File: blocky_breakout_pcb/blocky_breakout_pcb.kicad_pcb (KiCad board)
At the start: 4 copper layers, 85 x 61 mm, 91 parts, among them J1 Raspberry_Pi_4, J10 Conn_01x02_Pin, J11 Conn_01x02_Pin, J12 Conn_01x02_Pin, J2 USB_C_Receptacle_USB2.0_16P, J3 Conn_01x14_Pin, J4 Conn_01x08_Pin, J5 Conn_01x10_Pin, J6 Conn_01x06_Pin, J7 Conn_01x08_Pin, J9 Conn_01x03_Pin, K1 EE2-3TNUH, K2 EE2-3TNUH, Q1 DMG1012TQ-7, Q2 DMG1012TQ-7, SW1 SW_Push, SW2 SW_DIP_x04, U1 W25Q32JVSS, U2 NUP2202, U3 RP2350, U4 LM4040C33FTA, U5 LM66100DCK, U6 AOZ1280CI, U7 LM66100DCK, U8 MCP4728, U9 TCR2EE11, Y1 12Mhz

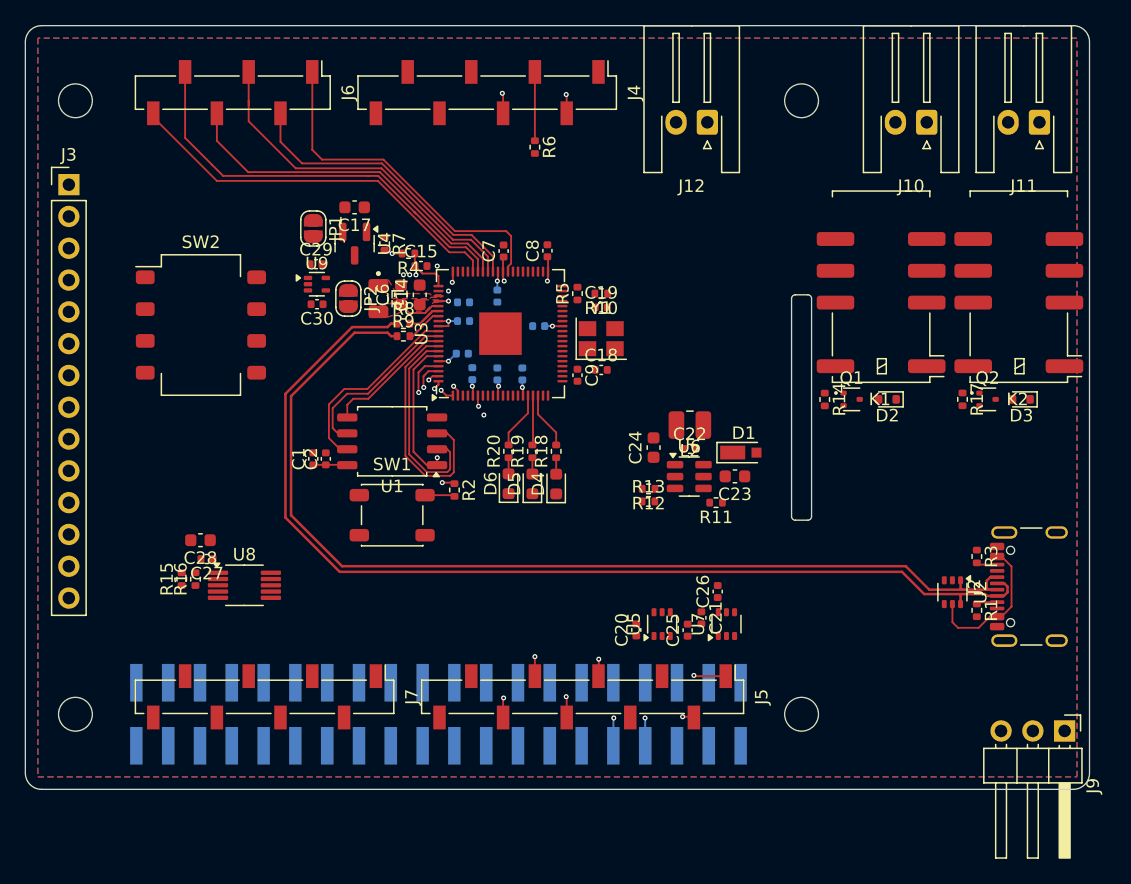
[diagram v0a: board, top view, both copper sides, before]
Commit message: Layout nearly finished, entering part numbers
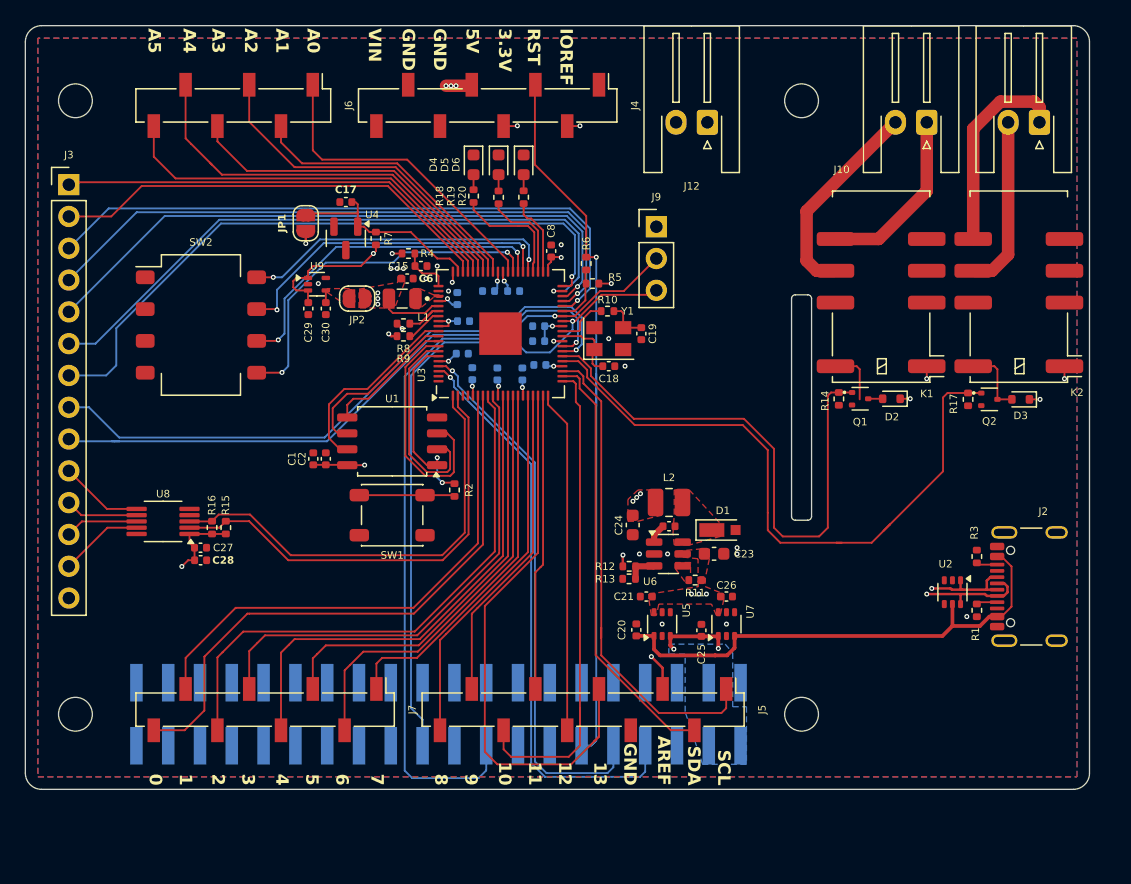
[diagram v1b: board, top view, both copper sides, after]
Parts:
- C14: footprint Capacitor_SMD:C_0603_1608Metric -> Capacitor_SMD:C_0402_1005Metric; moved to B.Cu
- C17, C28, C6: footprint Capacitor_SMD:C_0603_1608Metric -> Capacitor_SMD:C_0402_1005Metric
- C2: value 10nF -> 100nF
- C7, C9: moved to B.Cu
- J9: footprint Connector_PinHeader_2.54mm:PinHeader_1x03_P2.54mm_Horizontal -> Connector_PinHeader_2.54mm:PinHeader_1x03_P2.54mm_Vertical
- Y1: footprint Crystal:Crystal_SMD_Abracon_ABM8AIG-4Pin_3.2x2.5mm -> X_Abracon:Crystal_SMD_Abracon_ABM8-272-T3-4Pin_3.2x2.5mm
- moved J9 51.8 mm to (151.4, 82.1), turned to 0 degrees
- moved D4 26.3 mm to (136.8, 77.1), turned to -90 degrees
- moved D5 25.6 mm to (138.8, 77.1), turned to -90 degrees
- moved D6 25.5 mm to (140.8, 77.1), turned to -90 degrees
- moved R18 21.4 mm to (136.8, 79.6), turned to -90 degrees
- moved R19 20.5 mm to (138.8, 79.7), turned to -90 degrees
- moved R20 20.3 mm to (140.8, 79.7), turned to -90 degrees
- moved R6 10.2 mm to (145.8, 85.0)
- moved U8 8.26 mm to (112.0, 105.6), turned to 180 degrees
- moved C16 6.75 mm to (142.0, 91.2), turned to 180 degrees
- moved C22 6.41 mm to (152.4, 106.0)
- moved C23 6.41 mm to (156.0, 108.2)
- moved C24 6.41 mm to (149.5, 105.9)
- moved D1 6.41 mm to (156.7, 106.3)
- moved R11 6.41 mm to (154.5, 110.3)
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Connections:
- J1 pad 11: /RP2350/SWD_SWDIO -> unconnected-(J1-GPIO17/SPI1_~{CE1}-Pad11)
- J1 pad 18: unconnected-(J1-GPIO24/SDIO_DAT0-Pad18) -> /RP2350/SWD_SWDIO
- J1 pad 22: unconnected-(J1-GPIO25/SDIO_DAT1-Pad22) -> /RP2350/SWD_SWCLK
- J1 pad 36: /RP2350/SWD_SWCLK -> unconnected-(J1-GPIO16/SPI1_~{CE2}-Pad36)
- J3 pad 1: /RP2350/GPIO6 -> /RP2350/GPIO46
- J3 pad 10: /RP2350/GPIO30 -> /DAC/DAC0
- J3 pad 11: /RP2350/GPIO31 -> /DAC/DAC1
- J3 pad 12: /RP2350/GPIO46 -> /DAC/DAC2
- J3 pad 13: /RP2350/GPIO47 -> /DAC/DAC3
- J3 pad 2: /RP2350/GPIO7 -> /RP2350/GPIO47
- J3 pad 3: /RP2350/GPIO19 -> /RP2350/GPIO28
- J3 pad 4: /RP2350/GPIO23 -> /RP2350/GPIO29
- J3 pad 5: /RP2350/GPIO22 -> /RP2350/GPIO30
- J3 pad 6: /RP2350/GPIO26 -> /RP2350/GPIO31
- J3 pad 7: /RP2350/GPIO27 -> /RP2350/GPIO32
- J3 pad 8: /RP2350/GPIO28 -> /RP2350/GPIO26
- J3 pad 9: /RP2350/GPIO29 -> /RP2350/GPIO27
- J5 pad 1: /Arduino Headers/I2C0.SCL -> /Arduino Headers/I2C1.SCL
- J5 pad 2: /Arduino Headers/I2C0.SDA -> /Arduino Headers/I2C1.SDA
- Q1 pad 1: /RP2350/RELAY1_EN -> /RP2350/RELAY2_EN
- Q2 pad 1: /RP2350/RELAY2_EN -> /RP2350/RELAY1_EN
- R14 pad 1: /RP2350/RELAY1_EN -> /RP2350/RELAY2_EN
- R15 pad 1: /DAC/I2C1.SCL -> /DAC/I2C0.SCL
- R16 pad 1: /DAC/I2C1.SDA -> /DAC/I2C0.SDA
- R17 pad 1: /RP2350/RELAY2_EN -> /RP2350/RELAY1_EN
- R18 pad 2: /RP2350/GPIO18 -> /RP2350/GPIO35
- R19 pad 2: /RP2350/GPIO17 -> /RP2350/GPIO34
- R20 pad 2: /RP2350/GPIO16 -> /RP2350/GPIO33
- SW2 pad 5: /RP2350/GPIO12 -> /RP2350/GPIO39
- SW2 pad 6: /RP2350/GPIO13 -> /RP2350/GPIO38
- SW2 pad 7: /RP2350/GPIO14 -> /RP2350/GPIO37
- SW2 pad 8: /RP2350/GPIO15 -> /RP2350/GPIO36
- U3 pad 1: /Arduino Headers/SPI0.MISO -> /DAC/I2C0.SDA
- U3 pad 11: /RP2350/GPIO12 -> /Arduino Headers/D4
- U3 pad 12: /RP2350/GPIO13 -> /Arduino Headers/D5
- U3 pad 13: /RP2350/GPIO14 -> /Arduino Headers/D6
- U3 pad 14: /RP2350/GPIO15 -> /Arduino Headers/D7
- U3 pad 16: /RP2350/GPIO16 -> /Arduino Headers/D8
- U3 pad 17: /RP2350/GPIO17 -> /Arduino Headers/D9
- U3 pad 18: /RP2350/GPIO18 -> /Arduino Headers/SPI0.SCK
- U3 pad 19: /RP2350/GPIO19 -> /Arduino Headers/SPI0.MOSI
- U3 pad 2: /Arduino Headers/SPI0.CS -> /DAC/I2C0.SCL
- U3 pad 20: /Arduino Headers/D0/RX -> /Arduino Headers/SPI0.MISO
- U3 pad 21: /Arduino Headers/D1/TX -> /Arduino Headers/SPI0.CS
- U3 pad 22: /RP2350/GPIO22 -> /Arduino Headers/I2C1.SDA
- U3 pad 23: /RP2350/GPIO23 -> /Arduino Headers/I2C1.SCL
- U3 pad 40: /Arduino Headers/D2 -> /RP2350/GPIO32
- U3 pad 42: /Arduino Headers/D3 -> /RP2350/GPIO33
- U3 pad 43: /Arduino Headers/D4 -> /RP2350/GPIO34
- U3 pad 44: /Arduino Headers/D5 -> /RP2350/GPIO35
- U3 pad 45: /Arduino Headers/D6 -> /RP2350/GPIO36
- U3 pad 46: /Arduino Headers/D7 -> /RP2350/GPIO37
- U3 pad 47: /Arduino Headers/D8 -> /RP2350/GPIO38
- U3 pad 48: /Arduino Headers/D9 -> /RP2350/GPIO39
- U3 pad 6: /Arduino Headers/I2C0.SDA -> /Arduino Headers/D1/TX
- U3 pad 7: /Arduino Headers/I2C0.SCL -> /Arduino Headers/D0/RX
- U3 pad 79: /Arduino Headers/SPI0.SCK -> unconnected-(U3B-GPIO2-Pad79)
- U3 pad 8: /DAC/I2C1.SDA -> /Arduino Headers/D2
- U3 pad 80: /Arduino Headers/SPI0.MOSI -> unconnected-(U3B-GPIO3-Pad80)
- U3 pad 9: /DAC/I2C1.SCL -> /Arduino Headers/D3
- U8 pad 2: /DAC/I2C1.SCL -> /DAC/I2C0.SCL
- U8 pad 3: /DAC/I2C1.SDA -> /DAC/I2C0.SDA
- U8 pad 6: unconnected-(U8-VOUTA-Pad6) -> /DAC/DAC0
- U8 pad 7: unconnected-(U8-VOUTB-Pad7) -> /DAC/DAC1
- U8 pad 8: unconnected-(U8-VOUTC-Pad8) -> /DAC/DAC2
- U8 pad 9: unconnected-(U8-VOUTD-Pad9) -> /DAC/DAC3
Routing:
- net +5V: track 0.00 -> 72.2 mm, vias 0 -> 7
- net /RP2350/SWD_SWDIO: track 0.00 -> 64.5 mm, vias 0 -> 1
- net /RP2350/SWD_SWCLK: track 0.00 -> 54.3 mm, vias 0 -> 1
- net /Arduino Headers/RST: track 5.49 -> 59.1 mm, vias 0 -> 1
- net /RP2350/RELAY1_EN: track 0.00 -> 53.1 mm
- net /RP2350/GPIO32: track 0.00 -> 52.4 mm, vias 0 -> 1
- net /RP2350/GPIO31: track 0.00 -> 51.9 mm, vias 0 -> 1
- net /RP2350/GPIO28: track 0.00 -> 51.2 mm, vias 0 -> 1
- net /RP2350/GPIO29: track 0.00 -> 51.0 mm, vias 0 -> 1
- net /RP2350/GPIO30: track 0.00 -> 50.8 mm, vias 0 -> 1
- net /RP2350/GPIO26: track 0.00 -> 50.6 mm, vias 0 -> 1
- net /RP2350/GPIO27: track 0.00 -> 49.1 mm, vias 0 -> 1
- net /Arduino Headers/AREF: track 0.00 -> 48.4 mm, vias 0 -> 2
- net /Arduino Headers/D0/RX: track 0.00 -> 46.9 mm
- net /Arduino Headers/D2: track 0.00 -> 44.2 mm
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- added copper zone on In1.Cu, net +1V1
- added copper zone on F.Cu, net +5V
- added copper zone on B.Cu, net +5V_RPI
- added copper zone on F.Cu, net Net-(D1-K)
- added copper zone on F.Cu, net Net-(JP2-A)
- added copper zone on F.Cu, net Net-(U6-EN)
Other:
- board text added: "0"
- board text added: "1"
- board text added: "10"
- board text added: "11"
- board text added: "12"
- board text added: "13"
- board text added: "2"
- board text added: "3"
- board text added: "3.3V"
- board text added: "4"
- board text added: "5"
- board text added: "5V"
- board text added: "6"
- board text added: "7"
- board text added: "8"
- board text added: "9"
- board text added: "A0"
- board text added: "A1"
- board text added: "A2"
- board text added: "A3"
- board text added: "A4"
- board text added: "A5"
- board text added: "AREF"
- board text added: "GND"
- board text added: "IOREF"
- board text added: "RST"
- board text added: "SCL"
- board text added: "SDA"
- board text added: "VIN"

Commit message: Added some docs, worked on routing.
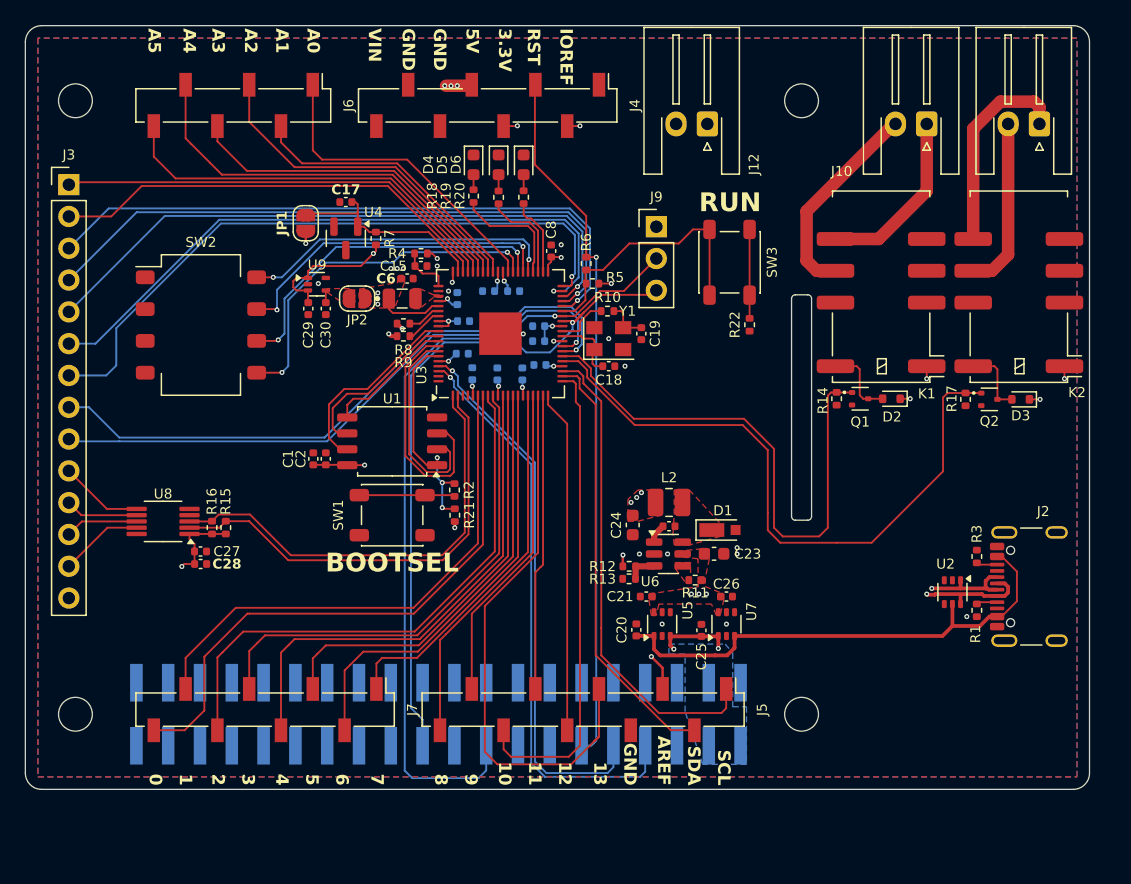
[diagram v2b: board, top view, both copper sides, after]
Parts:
- added R21: 10k, Resistor_SMD:R_0402_1005Metric, F.Cu at (135.3, 105.1)
- added R22: 1k, Resistor_SMD:R_0402_1005Metric, F.Cu at (158.8, 89.9)
- added SW3: SW_Push, Button_Switch_SMD:SW_SPST_PTS647_Sx38, F.Cu at (157.2, 84.9)
- moved R4 1.00 mm to (132.6, 84.2), turned to 0 degrees
- moved C27 0.30 mm to (115.0, 108.0)
- moved C28 0.30 mm to (115.0, 109.0)
- moved R17 0.20 mm to (176.1, 95.8)
- moved R14 0.18 mm to (165.8, 95.8)
- moved J10 0.13 mm to (173.0, 73.8)
- moved J11 0.13 mm to (182.0, 73.8)
- moved J12 0.13 mm to (155.5, 73.8)
- turned L1 to 0 degrees
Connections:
- L1 pad 1: /RP2350/VREF_LX -> +1V1
- L1 pad 2: +1V1 -> /RP2350/VREF_LX
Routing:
- net Net-(U3A-RUN): track 4.65 -> 21.1 mm
- net Net-(R22-Pad2): track 0.00 -> 7.10 mm
- net /RP2350/QSPI_~{SS}: track 15.1 -> 18.1 mm, vias 2 -> 3
- net /RP2350/SWD_SWCLK: track 54.3 -> 57.3 mm
- net /Arduino Headers/RST: track 59.1 -> 56.5 mm
- net /Arduino Headers/SPI0.CS: track 41.1 -> 39.1 mm
- net Net-(U3A-USB_DM): track 3.84 -> 2.70 mm
- net /RP2350/RELAY1_EN: track 53.1 -> 52.0 mm
- net V_USB: track 41.2 -> 40.2 mm
- net +3V3: track 34.2 -> 35.1 mm, vias 24 -> 25
- net /Arduino Headers/I2C1.SCL: track 39.1 -> 38.3 mm
- net /RP2350/GPIO27: track 49.1 -> 48.5 mm
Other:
- board text added: "BOOTSEL"
- board text added: "RUN"
